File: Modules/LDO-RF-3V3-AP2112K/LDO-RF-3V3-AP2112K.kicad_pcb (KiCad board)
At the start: 4 copper layers, 3 parts, among them U9 AP2112K-3.3

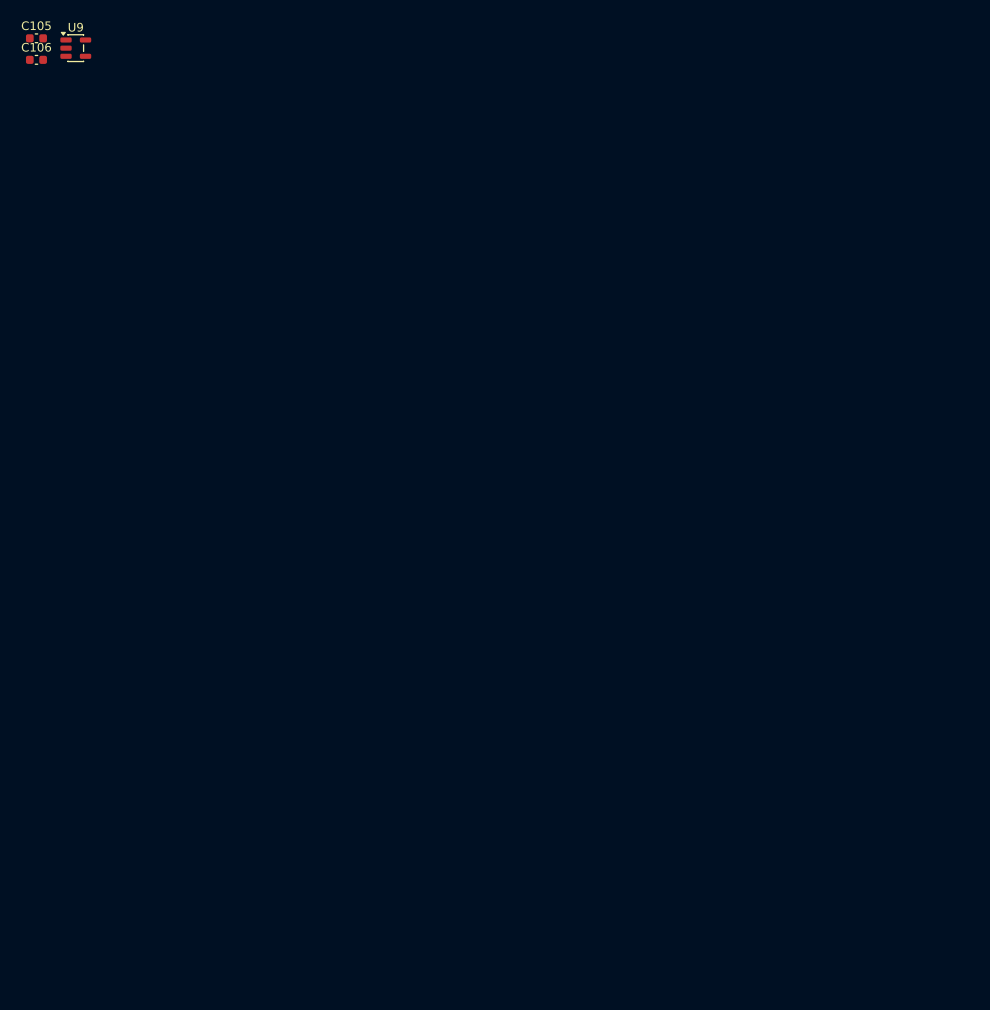
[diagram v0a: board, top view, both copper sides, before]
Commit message: Lay out the LDO-RF-3V3-AP2112K module
10 x 12 mm, 4 layers. C105 sits 0.6 mm west of the draft position so the
F.Cu pour reaches U9.2 with two spokes. EN reaches V5_SYS through the In2
plane. Breakout row at y 109.5 with V5_SYS and +3V3_RF stubs.

DRC: 0 errors, 0 unconnected, 0 parity. The 2 track_dangling warnings are
the 2 interface stubs. Canary 7 to 61.

Co-Authored-By: Claude Opus 5.5 (1M context) <noreply@anthropic.com>
Claude-Session: https://claude.ai/code/session_01ErAAfkmF4h3T5yfrw21utF
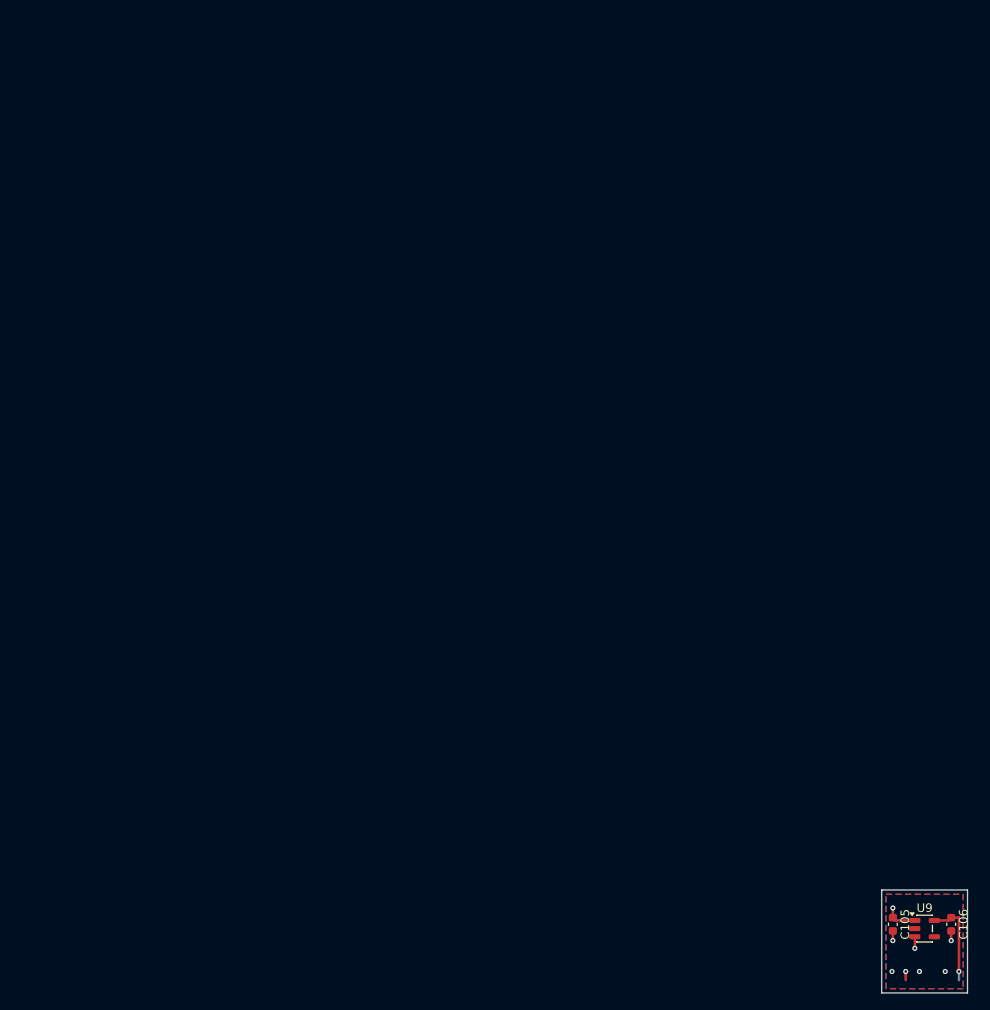
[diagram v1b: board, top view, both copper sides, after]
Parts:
- moved C106 146.7 mm to (108.1, 104.0), turned to -90 degrees
- moved C105 143.6 mm to (101.3, 104.0), turned to -90 degrees
- moved U9 142.5 mm to (105.0, 104.5)
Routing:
- net /+3V3_RF: track 0.00 -> 10.3 mm, vias 0 -> 1
- net /V5_SYS: track 0.00 -> 6.17 mm, vias 0 -> 3
- net GND: track 0.00 -> 2.25 mm, vias 0 -> 5
- added copper zone on In2.Cu, net /V5_SYS
- added copper zone on B.Cu, net GND
- added copper zone on F.Cu, net GND
- added copper zone on In1.Cu, net GND
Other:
- board outline added: 10 x 12 mm
- board text added: "+3V3_RF"
- board text added: "GND"
- board text added: "V5_SYS"

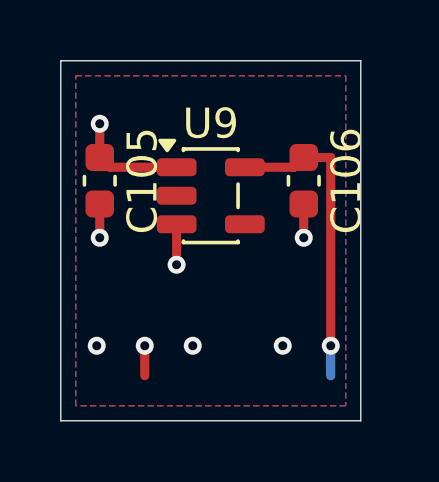
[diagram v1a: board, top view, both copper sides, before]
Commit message: Restore footprints and move passive references to F.Fab
GUI batch 2a on all eight module boards. Update Footprints from Library
restores the (units) blocks that Konnect IPC writes dropped: U10, U1, SW1,
SW2 and U4 no longer report lib_footprint_mismatch. Reference designators of
C, R, L, FB, D, Y and TP parts move to F.Fab. U, J and SW stay on the silk.

Every board: DRC 0 errors, 0 unconnected, 0 parity, the canary fires, and
track_dangling equals the interface stub count.

Co-Authored-By: Claude Opus 5.5 (1M context) <noreply@anthropic.com>
Claude-Session: https://claude.ai/code/session_01ErAAfkmF4h3T5yfrw21utF
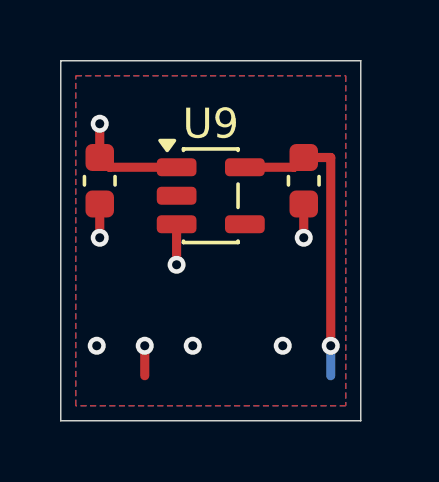
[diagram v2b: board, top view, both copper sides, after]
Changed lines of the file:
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@@
 		(tags "capacitor")
 		(property "Reference" "C106"
-			(at 0 -1.43 -90)
-			(layer "F.SilkS")
+			(at 0 -1.43 270)
+			(layer "F.Fab")
 			(effects
 				(font
@@
 		)
 		(property "Value" "1uF"
-			(at 0 1.43 -90)
+			(at 0 1.43 270)
 			(layer "F.Fab")
 			(effects
@@
 		)
 		(property "Datasheet" ""
-			(at 0 0 -90)
+			(at 0 0 270)
 			(layer "F.Fab")
 			(hide yes)
@@
 		)
 		(property "Description" ""
-			(at 0 0 -90)
+			(at 0 0 270)
 			(layer "F.Fab")
 			(hide yes)
@@
 		)
 		(property "KiLib_Generator" "SMD_2terminal_chip_molded"
-			(at 0 0 -90)
+			(at 0 0 270)
 			(layer "F.SilkS")
 			(hide yes)
@@
 		)
 		(property "MPN" "GRM188R71E105KA12D"
-			(at 0 0 -90)
+			(at 0 0 270)
 			(unlocked yes)
 			(layer "F.Fab")
@@
 		)
 		(property "Manufacturer" "Murata"
-			(at 0 0 -90)
+			(at 0 0 270)
 			(unlocked yes)
 			(layer "F.Fab")
@@
 		)
 		(fp_text user "${REFERENCE}"
-			(at 0 0 -90)
+			(at 0 0 270)
 			(layer "F.Fab")
 			(effects
@@
 		(tags "capacitor")
 		(property "Reference" "C105"
-			(at 0 -1.43 -90)
-			(layer "F.SilkS")
+			(at 0 -1.43 270)
+			(layer "F.Fab")
 			(effects
 				(font
@@
 		)
 		(property "Value" "1uF"
-			(at 0 1.43 -90)
+			(at 0 1.43 270)
 			(layer "F.Fab")
 			(effects
@@
 		)
 		(property "Datasheet" ""
-			(at 0 0 -90)
+			(at 0 0 270)
 			(layer "F.Fab")
 			(hide yes)
@@
 		)
 		(property "Description" ""
-			(at 0 0 -90)
+			(at 0 0 270)
 			(layer "F.Fab")
 			(hide yes)
@@
 		)
 		(property "KiLib_Generator" "SMD_2terminal_chip_molded"
-			(at 0 0 -90)
+			(at 0 0 270)
 			(layer "F.SilkS")
 			(hide yes)
@@
 		)
 		(property "MPN" "GRM188R71E105KA12D"
-			(at 0 0 -90)
+			(at 0 0 270)
 			(unlocked yes)
 			(layer "F.Fab")
@@
 		)
 		(property "Manufacturer" "Murata"
-			(at 0 0 -90)
+			(at 0 0 270)
 			(unlocked yes)
 			(layer "F.Fab")
@@
 		)
 		(fp_text user "${REFERENCE}"
-			(at 0 0 -90)
-			(layer "F.Fab")
-			(effects
+			(at 0 0 270)
+			(layer "F.Fab")
+			(effects
